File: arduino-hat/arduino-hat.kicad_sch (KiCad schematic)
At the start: 10 parts, among them Q1 MMBT2222A, Q2 MMBT2222A, Q3 MMBT2222A, Q4 MMBT2222A

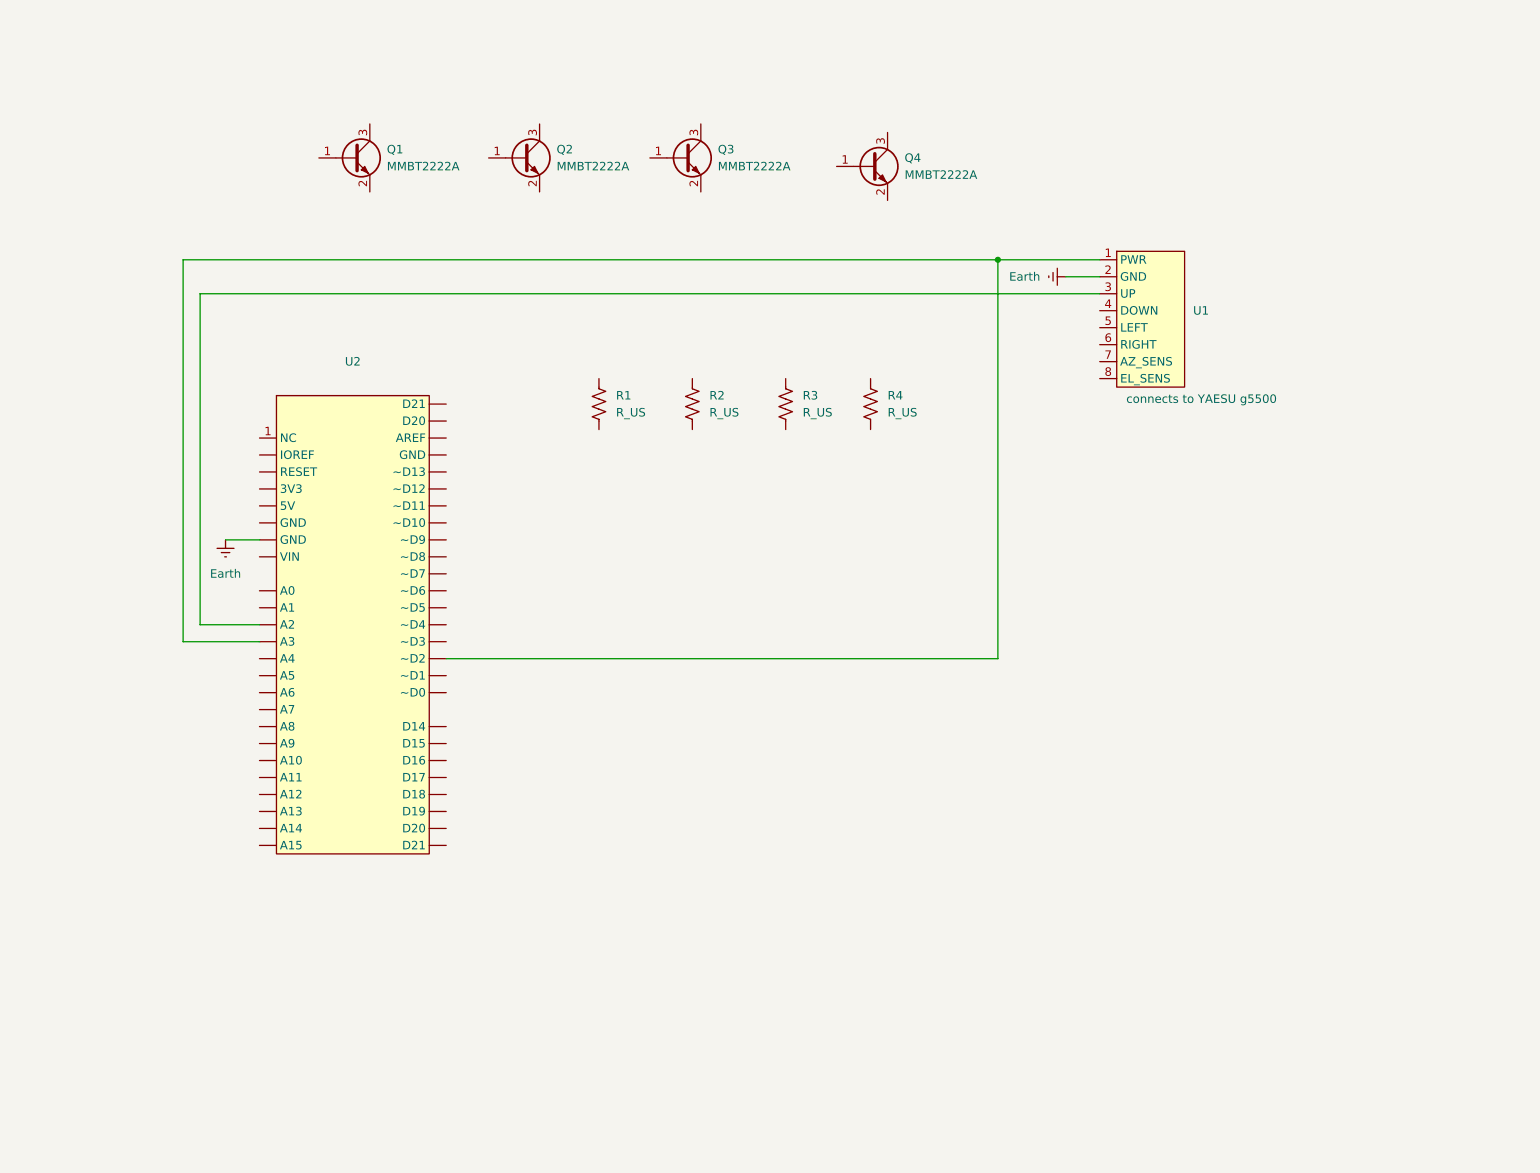
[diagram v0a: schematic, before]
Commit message: imported arduino docs
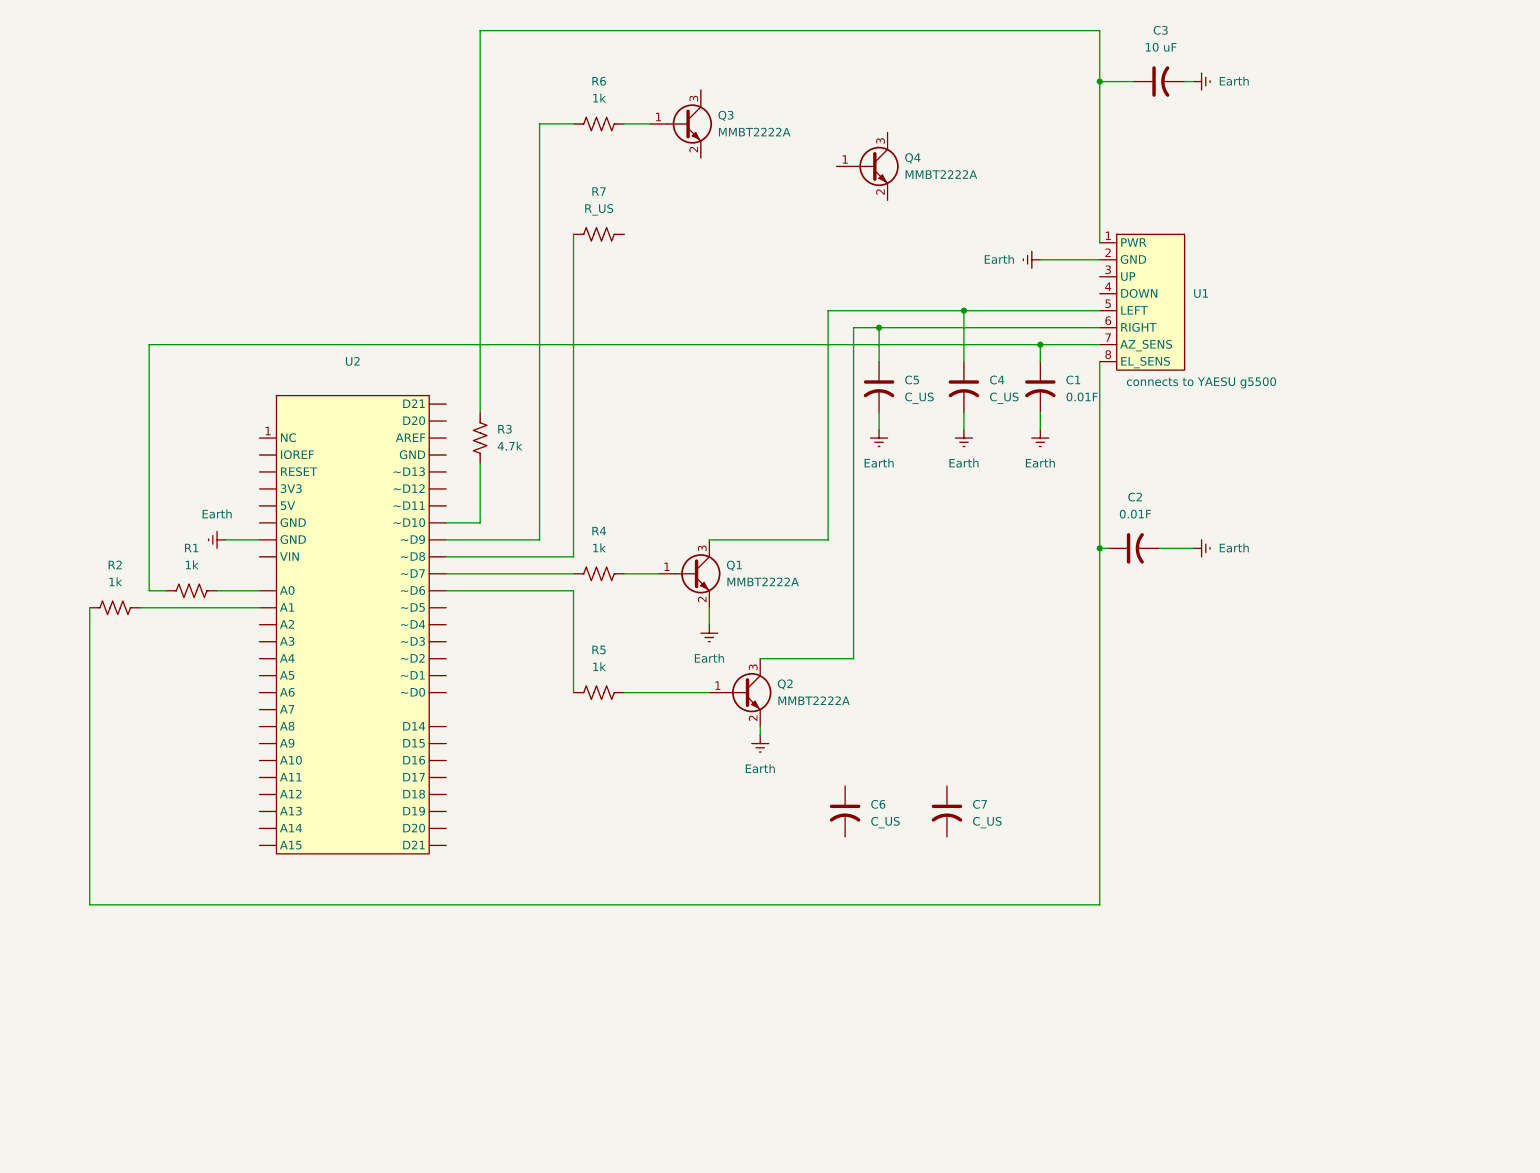
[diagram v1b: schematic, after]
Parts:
- added C1, C2: 0.01F, symbol Device:C_US
- added C3: 10 uF, symbol Device:C_US
- added C4, C5, C6, C7: C_US, symbol Device:C_US
- added R5, R6: 1k, symbol Device:R_US
- added R7: R_US, symbol Device:R_US
- R1, R2, R4: value R_US -> 1k
- R3: value R_US -> 4.7k
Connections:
- net Earth: now also Q1.2 (E), Q2.2 (E), C1.2, C2.2, C3.2, C4.2, C5.2
- net at R1.1: now also U1.7 (AZ_SENS), C1.1
- net at R1.2: now also U2. (D21)
- net at R2.1: now also U1.8 (EL_SENS), C2.1
- net at R2.2: now also U2. (D21)
- net at R4.1: now also U2. (D21)
- net at R4.2: now also Q1.1 (B)
- net at U1.1 (PWR): now also R3.1, C3.1; no longer U2. (D21)
- net at U1.3 (UP): no longer U2. (D21)
- net at Q1.3 (C): now also U1.5 (LEFT), C4.1
- net at Q3.1 (B): now also R6.2
- net at Q2.1 (B): now also R5.2
- net at Q2.3 (C): now also U1.6 (RIGHT), C5.1
- net at R3.2: now also U2. (D21)
- new net: R5.1, U2. (D21)
- new net: R6.1, U2. (D21)
- new net: R7.1, U2. (D21)
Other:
- moved on the sheet: Q1, Q2, Q3, R1, R2, R3, R4, U1

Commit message: Update arduino-hat.kicad_sch
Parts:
- removed C6, C7: C_US, symbol Device:C_US
- added C8, C9: 0.01, symbol Device:C_US
- C4, C5: value C_US -> 0.01
- R7: value R_US -> 1k
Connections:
- net Earth: now also Q3.2 (E), Q4.2 (E), C8.2, C9.2
- net at Q4.1 (B): now also R7.2
- net at Q4.3 (C): now also U1.3 (UP), C9.1
- net at Q3.3 (C): now also U1.4 (DOWN), C8.1
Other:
- moved on the sheet: Q4, R7

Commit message: finished schematic?
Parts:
- removed U2: ~, symbol connectors:arduinoMEGA_hat_pins
- added A1: Arduino_Mega2560_R3_Shield, PCM_arduino-library:Arduino_Mega2560_R3_Shield, symbol PCM_arduino-library:Arduino_Mega2560_R3_Shield
- added D1: LED, LED_SMD:LED_1210_3225Metric_Pad1.42x2.65mm_HandSolder, symbol Device:LED
- added R8: 1k, Resistor_SMD:R_1210_3225Metric_Pad1.30x2.65mm_HandSolder, symbol Device:R_US
- C1, C2, C3, C4, C5, C8, C9: footprint (none) -> Capacitor_SMD:C_1210_3225Metric_Pad1.33x2.70mm_HandSolder
- R1, R2, R3, R4, R5, R6, R7: footprint (none) -> Resistor_SMD:R_1210_3225Metric_Pad1.30x2.65mm_HandSolder
- U1: footprint (none) -> Connector_PinHeader_2.54mm:PinHeader_1x08_P2.54mm_Vertical
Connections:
- net Earth: now also A1.GND1 (GND), A1.GND2 (GND), A1.GND3 (GND), A1.GND5 (GND), A1.GND6 (GND), D1.1 (K)
- net at C1.1, U1.7 (AZ_SENS): now also R1.2; no longer R1.1
- net at R2.2: now also A1.A1
- net at R5.1: now also A1.D6
- net at R4.1: now also A1.D7
- net at R6.1: now also A1.D9
- net at R3.2: now also A1.D10
- net at R7.1: now also A1.D8
- new net: A1.A0, R1.1
- new net: A1.D42, R8.2
- new net: D1.2 (A), R8.1
- no-connect marks 0 -> 78
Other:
- moved on the sheet: C1, C2, C3, C4, C5, C8, C9, Q1, Q2, Q3, Q4, R1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

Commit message: PCB design semi-finalized
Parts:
- removed C3: 10 uF, Capacitor_SMD:C_1210_3225Metric_Pad1.33x2.70mm_HandSolder, symbol Device:C_US
- removed R3: 4.7k, Resistor_SMD:R_1210_3225Metric_Pad1.30x2.65mm_HandSolder, symbol Device:R_US
- A1: footprint PCM_arduino-library:Arduino_Mega2560_R3_Shield -> PCM_arduino-library:Arduino_Mega2560_R3_Shield_revised
- C1, C2, C4, C5, C8, C9: footprint Capacitor_SMD:C_1210_3225Metric_Pad1.33x2.70mm_HandSolder -> Capacitor_SMD:C_0805_2012Metric_Pad1.18x1.45mm_HandSolder
- R1, R2, R4, R5, R6, R7, R8: footprint Resistor_SMD:R_1210_3225Metric_Pad1.30x2.65mm_HandSolder -> Resistor_SMD:R_0603_1608Metric_Pad0.98x0.95mm_HandSolder
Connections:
- no-connect marks 78 -> 80
